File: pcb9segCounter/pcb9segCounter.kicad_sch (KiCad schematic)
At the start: 0 parts

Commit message: Making progress, figuring out microcontroller interfacing
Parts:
- added J1: SAO, Connector_PinHeader_2.54mm:PinHeader_2x03_P2.54mm_Vertical, symbol Connector_Generic:Conn_02x03_Odd_Even
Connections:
- new net +5V: J1.1 (Pin_1)
- new net GND: J1.2 (Pin_2)
- new net GP1: J1.5 (Pin_5)
- new net GP2: J1.6 (Pin_6)
- new net SCL: J1.4 (Pin_4)
- new net SDA: J1.3 (Pin_3)
- no-connect marks 0 -> 1
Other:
- added sheet pcb9SegDigit1 (9SegDigit.kicad_sch)
- added sheet pcb9SegDigit2 (9SegDigit.kicad_sch)
- added sheet pcb9SegDigit3 (9SegDigit.kicad_sch)
- added sheet uC (uC.kicad_sch)

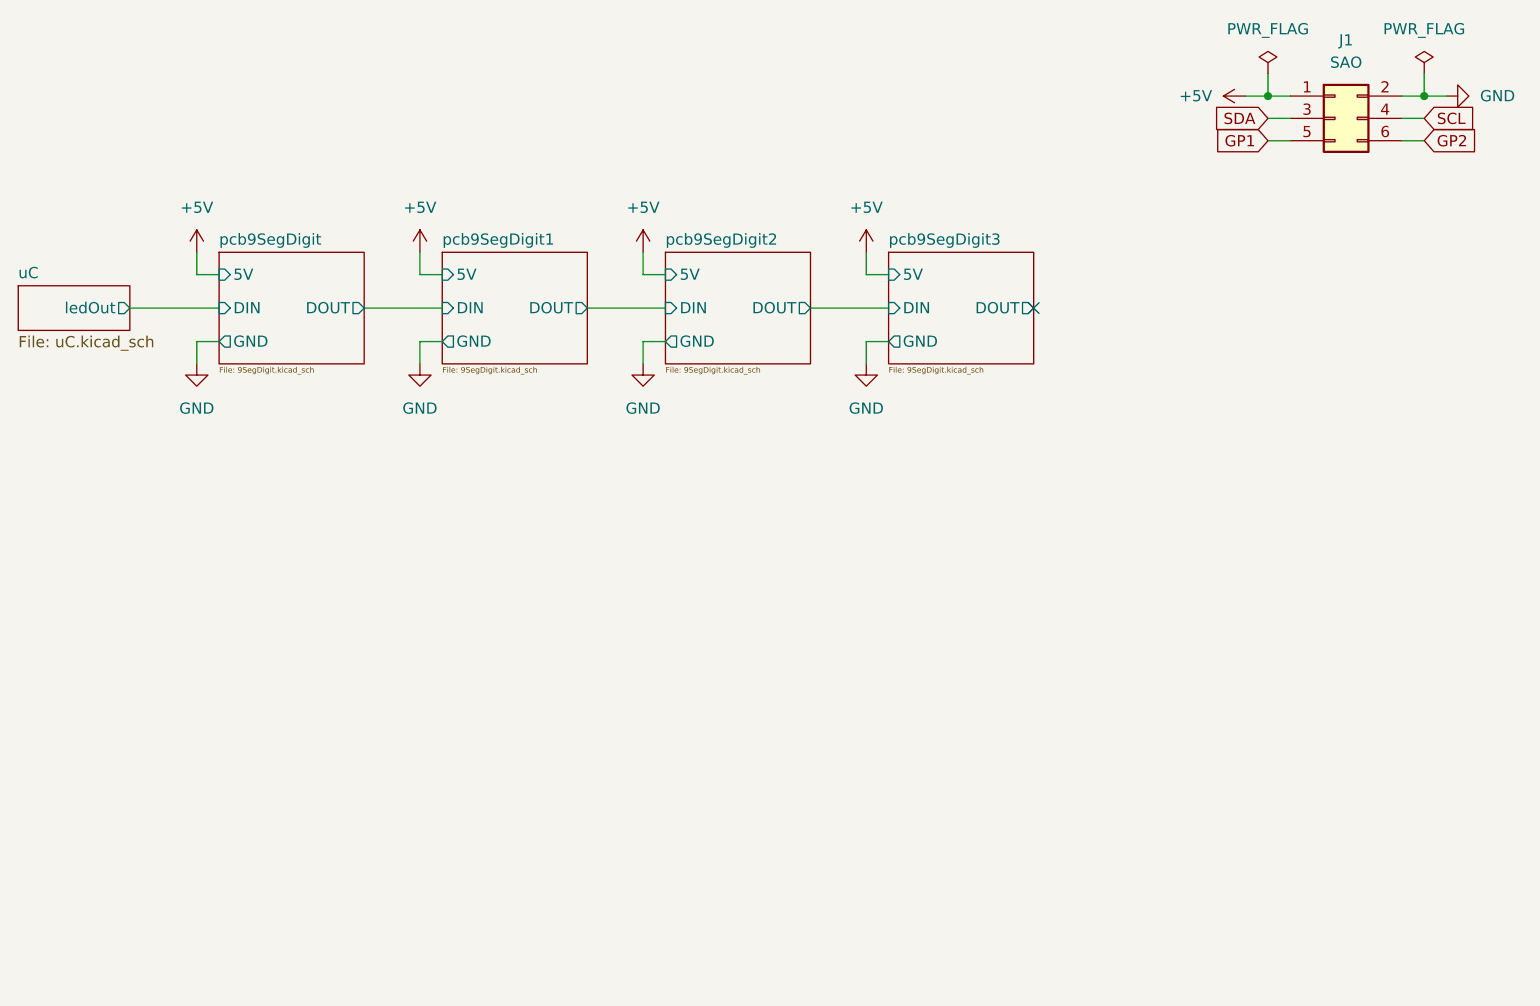
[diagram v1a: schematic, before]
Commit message: Schematic looks good, going to branch to reduce the number of digits from 4 to 2
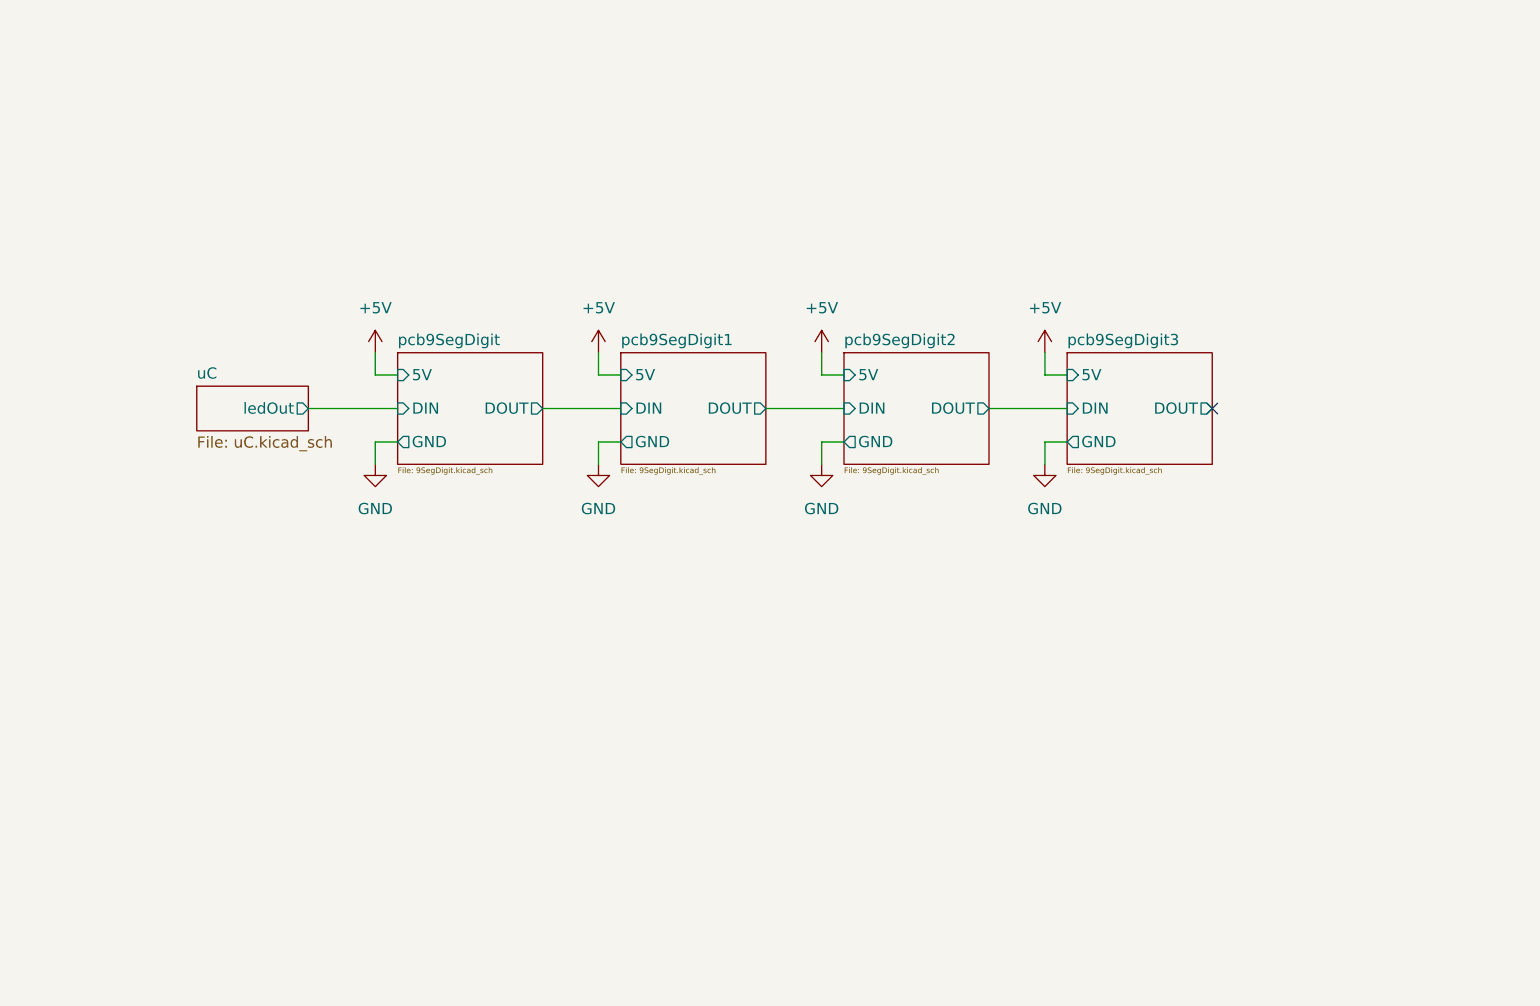
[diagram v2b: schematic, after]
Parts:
- removed J1: SAO, Connector_PinHeader_2.54mm:PinHeader_2x03_P2.54mm_Vertical, symbol Connector_Generic:Conn_02x03_Odd_Even

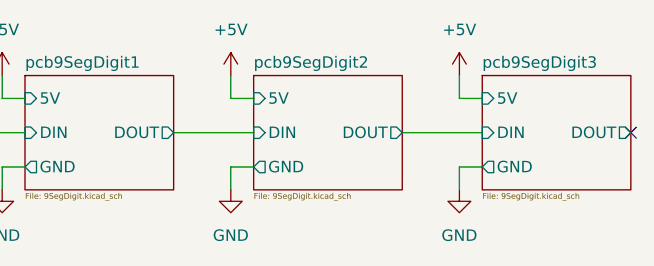
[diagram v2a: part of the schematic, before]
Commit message: reduced to 2 digits, added capacitors
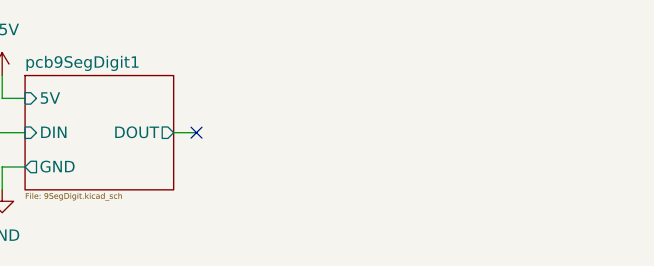
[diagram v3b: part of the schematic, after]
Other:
- removed sheet pcb9SegDigit2
- removed sheet pcb9SegDigit3

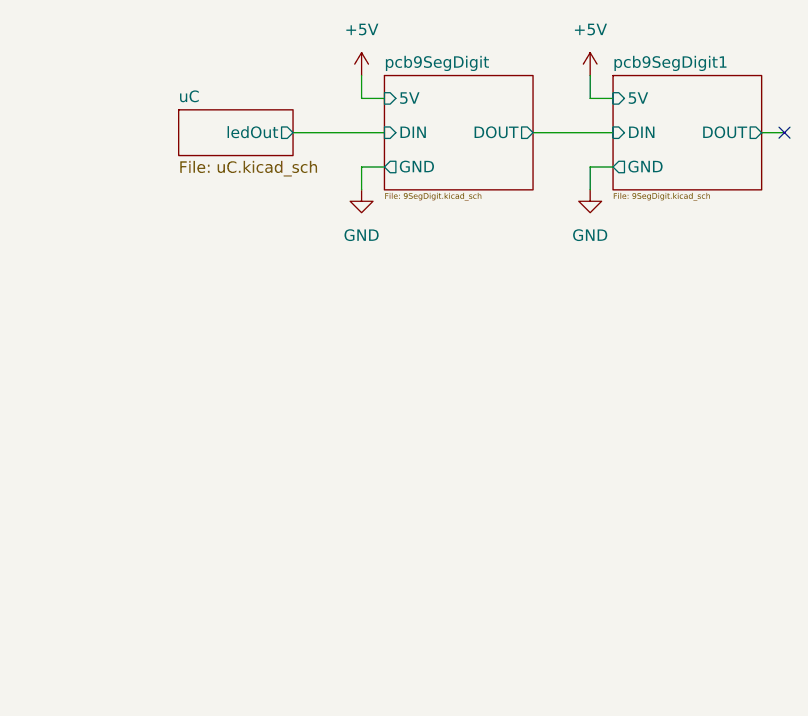
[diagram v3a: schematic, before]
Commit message: good routing, need to add slikscreen details
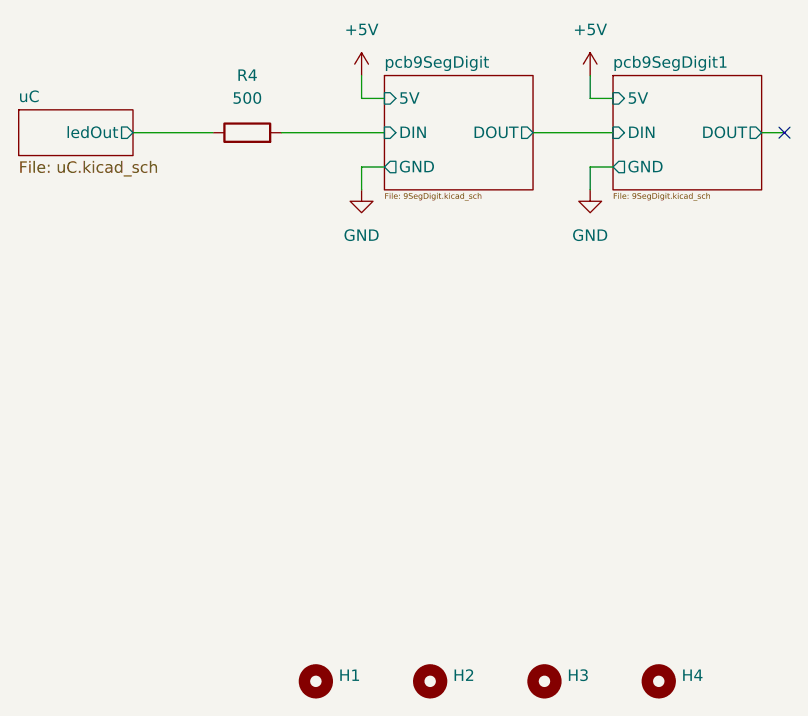
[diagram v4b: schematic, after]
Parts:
- added H1, H2, H3, H4: ~, MountingHole:MountingHole_2.2mm_M2_ISO7380, symbol Mechanical:MountingHole
- added R4: 500, Resistor_SMD:R_0805_2012Metric, symbol Device:R
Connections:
- net pcb9SegDigit/DIN: now also R4.2
- new net uC/ledOut: R4.1

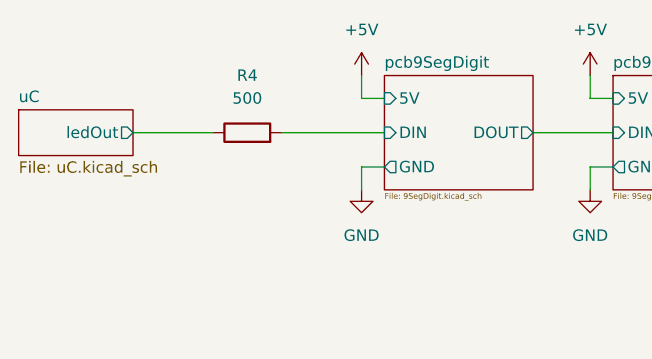
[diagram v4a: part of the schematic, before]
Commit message: Looks really good, all footprints and implementation check out. Looking to move an LED and adding an additional decap capacitor
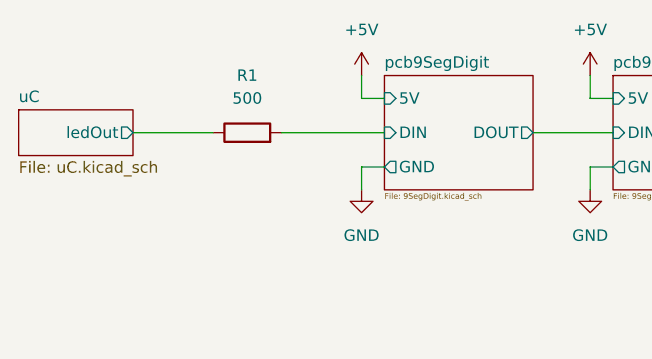
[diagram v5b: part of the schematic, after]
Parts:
- H1, H2, H3, H4: footprintCheck (none) -> y; implementationCheck (none) -> y
- R1: renamed from R4; footprintCheck (none) -> y; implementationCheck (none) -> y
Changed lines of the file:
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@@
+			)
+		)
+		(property "Footprint Check" ""
+			(at 114.3 127 0)
+			(effects
+				(font
+					(size 1.27 1.27)
+				)
+				(hide yes)
+			)
+		)
+		(property "Implementation" ""
+			(at 114.3 127 0)
+			(effects
+				(font
+					(size 1.27 1.27)
+				)
+				(hide yes)
+			)
+		)
+		(property "footprintCheck" "y"
+			(at 114.3 127 0)
+			(effects
+				(font
+					(size 1.27 1.27)
+				)
+				(hide yes)
+			)
+		)
+		(property "implementationCheck" "y"
+			(at 114.3 127 0)
+			(effects
+				(font
+					(size 1.27 1.27)
+				)
+				(hide yes)
 			)
 		)
@@
 			)
 		)
+		(property "Footprint Check" ""
+			(at 88.9 127 0)
+			(effects
+				(font
+					(size 1.27 1.27)
+				)
+				(hide yes)
+			)
+		)
+		(property "Implementation" ""
+			(at 88.9 127 0)
+			(effects
+				(font
+					(size 1.27 1.27)
+				)
+				(hide yes)
+			)
+		)
+		(property "footprintCheck" "y"
+			(at 88.9 127 0)
+			(effects
+				(font
+					(size 1.27 1.27)
+				)
+				(hide yes)
+			)
+		)
+		(property "implementationCheck" "y"
+			(at 88.9 127 0)
+			(effects
+				(font
+					(size 1.27 1.27)
+				)
+				(hide yes)
+			)
+		)
 		(instances
 			(project ""
@@
 			)
 		)
+		(property "Footprint Check" ""
+			(at 101.6 127 0)
+			(effects
+				(font
+					(size 1.27 1.27)
+				)
+				(hide yes)
+			)
+		)
+		(property "Implementation" ""
+			(at 101.6 127 0)
+			(effects
+				(font
+					(size 1.27 1.27)
+				)
+				(hide yes)
+			)
+		)
+		(property "footprintCheck" "y"
+			(at 101.6 127 0)
+			(effects
+				(font
+					(size 1.27 1.27)
+				)
+				(hide yes)
+			)
+		)
+		(property "implementationCheck" "y"
+			(at 101.6 127 0)
+			(effects
+				(font
+					(size 1.27 1.27)
+				)
+				(hide yes)
+			)
+		)
 		(instances
 			(project "pcb9segCounter"
@@
 			)
 		)
+		(property "Footprint Check" ""
+			(at 127 127 0)
+			(effects
+				(font
+					(size 1.27 1.27)
+				)
+				(hide yes)
+			)
+		)
+		(property "Implementation" ""
+			(at 127 127 0)
+			(effects
+				(font
+					(size 1.27 1.27)
+				)
+				(hide yes)
+			)
+		)
+		(property "footprintCheck" "y"
+			(at 127 127 0)
+			(effects
+				(font
+					(size 1.27 1.27)
+				)
+				(hide yes)
+			)
+		)
+		(property "implementationCheck" "y"
+			(at 127 127 0)
+			(effects
+				(font
+					(size 1.27 1.27)
+				)
+				(hide yes)
+			)
+		)
 		(instances
 			(project "pcb9segCounter"
@@
 		(dnp no)
 		(fields_autoplaced yes)
-		(property "Reference" "R4"
+		(property "Reference" "R1"
 			(at 81.28 59.69 90)
 			(effects
@@
 			)
 		)
+		(property "Footprint Check" ""
+			(at 81.28 66.04 0)
+			(effects
+				(font
+					(size 1.27 1.27)
+				)
+				(hide yes)
+			)
+		)
+		(property "Implementation" ""
+			(at 81.28 66.04 0)
+			(effects
+				(font
+					(size 1.27 1.27)
+				)
+				(hide yes)
+			)
+		)
+		(property "footprintCheck" "y"
+			(at 81.28 66.04 0)
+			(effects
+				(font
+					(size 1.27 1.27)
+				)
+				(hide yes)
+			)
+		)
+		(property "implementationCheck" "y"
+			(at 81.28 66.04 0)
+			(effects
+				(font
+					(size 1.27 1.27)
+				)
+				(hide yes)
+			)
+		)
 		(pin "2"
 		)
@@
 			(project ""
 				(path "/c50b0073-6340-498a-8f0c-212ef3b3c0fe"
-					(reference "R4")
-					(unit 1)
-				)
+					(reference "R1")
+					(unit 1)
+				)

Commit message: Doing lots of cleanup
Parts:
- R1: value 500 -> 470
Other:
- note added: "Electrical Elements"
- note added: "Mechanical Elements"
- company: (none) -> Ryan Martin
- title: (none) -> Nine Segment SAO
- moved on the sheet: H1, H2, H3, H4, R1
